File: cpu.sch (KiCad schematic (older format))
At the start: 26 parts, among them SW1 RESET, U1 74HC04, U2 Z80CPU, Y1 7.3728MHz

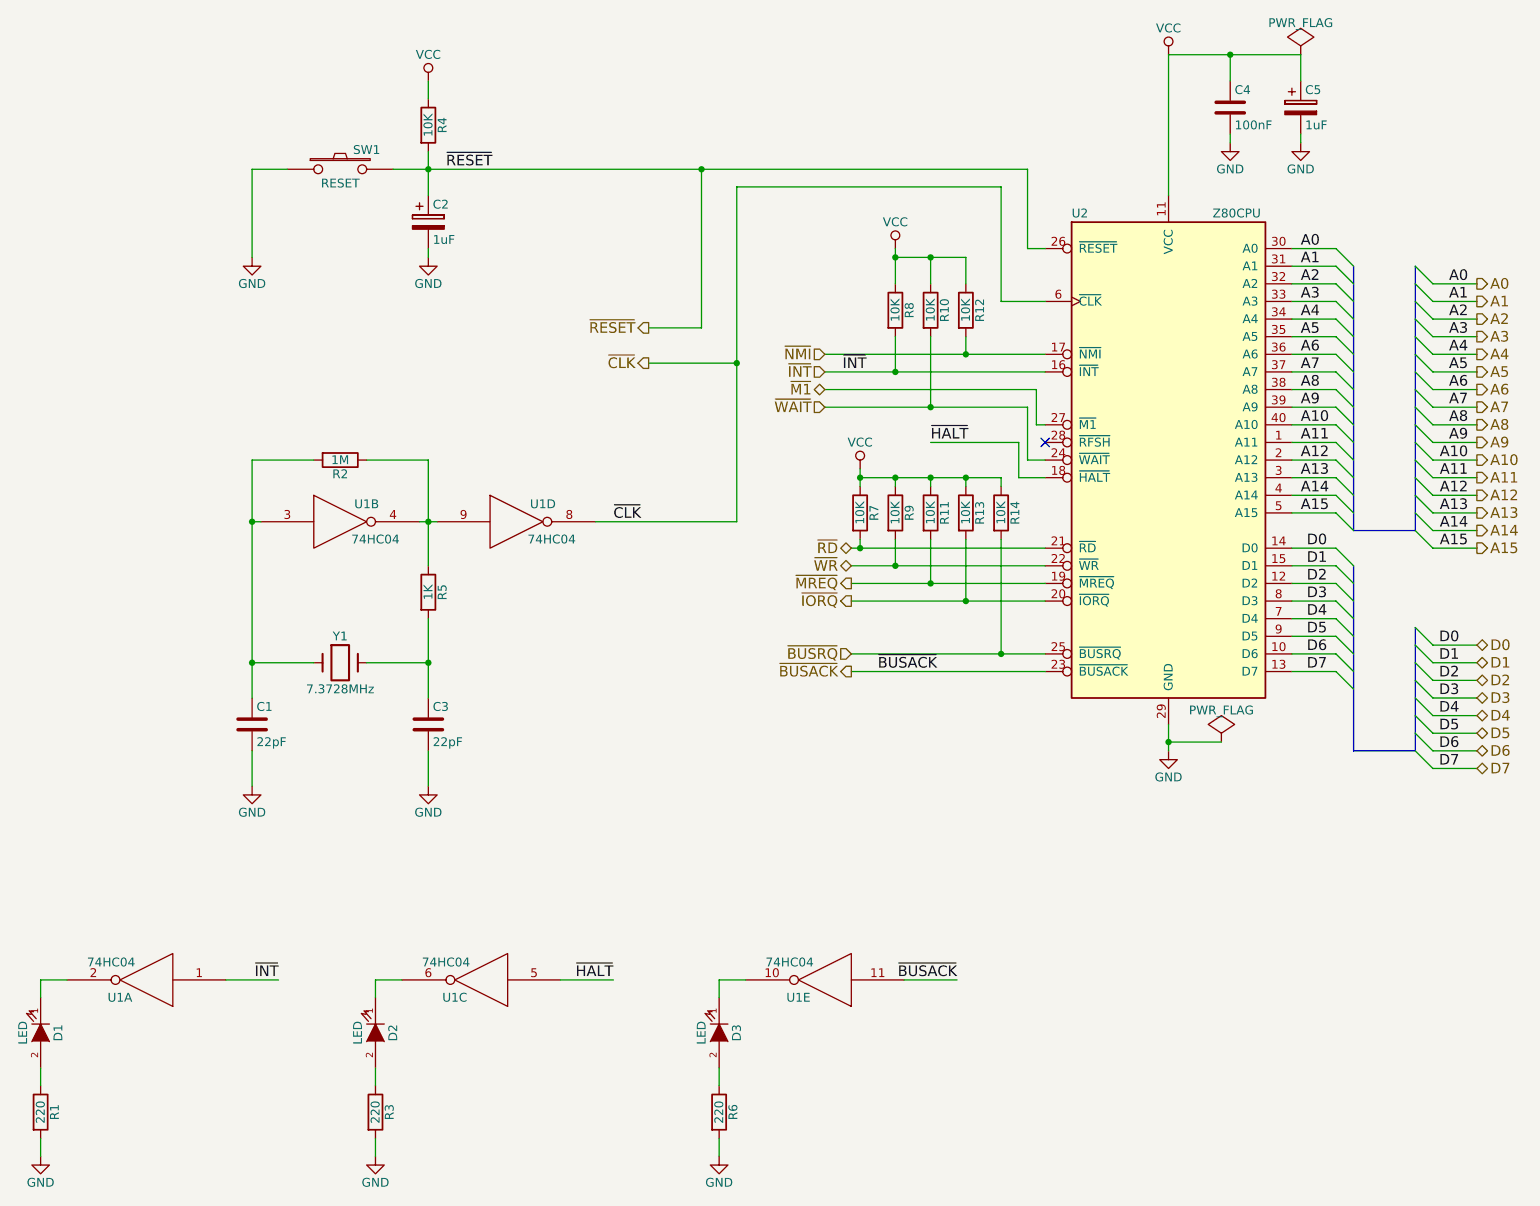
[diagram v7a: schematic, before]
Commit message: Added /intack signal and a pri-encoder for /iosel
Brain fart on the diode crap. Was tired. Added a priority encoder to
enable the Dx buffer so it properly tristates when no IObus ports are
selected.

Added a NOR gate to provide a /intack signal for any board to properly
detect their interupt has been accepted but the z80. Boards will need to
figure out who the interupt is for.

Will have to add interupt priority pins to the boards to allow the
boards to put jump vectors onto the data bus to service the interrupt
This should be fairly easy, just means the service pritority of the
slots will be A-H, with A being the highest priority and H being the
lowest.

Going to replace the hex inverters with the spare NOR gates too.
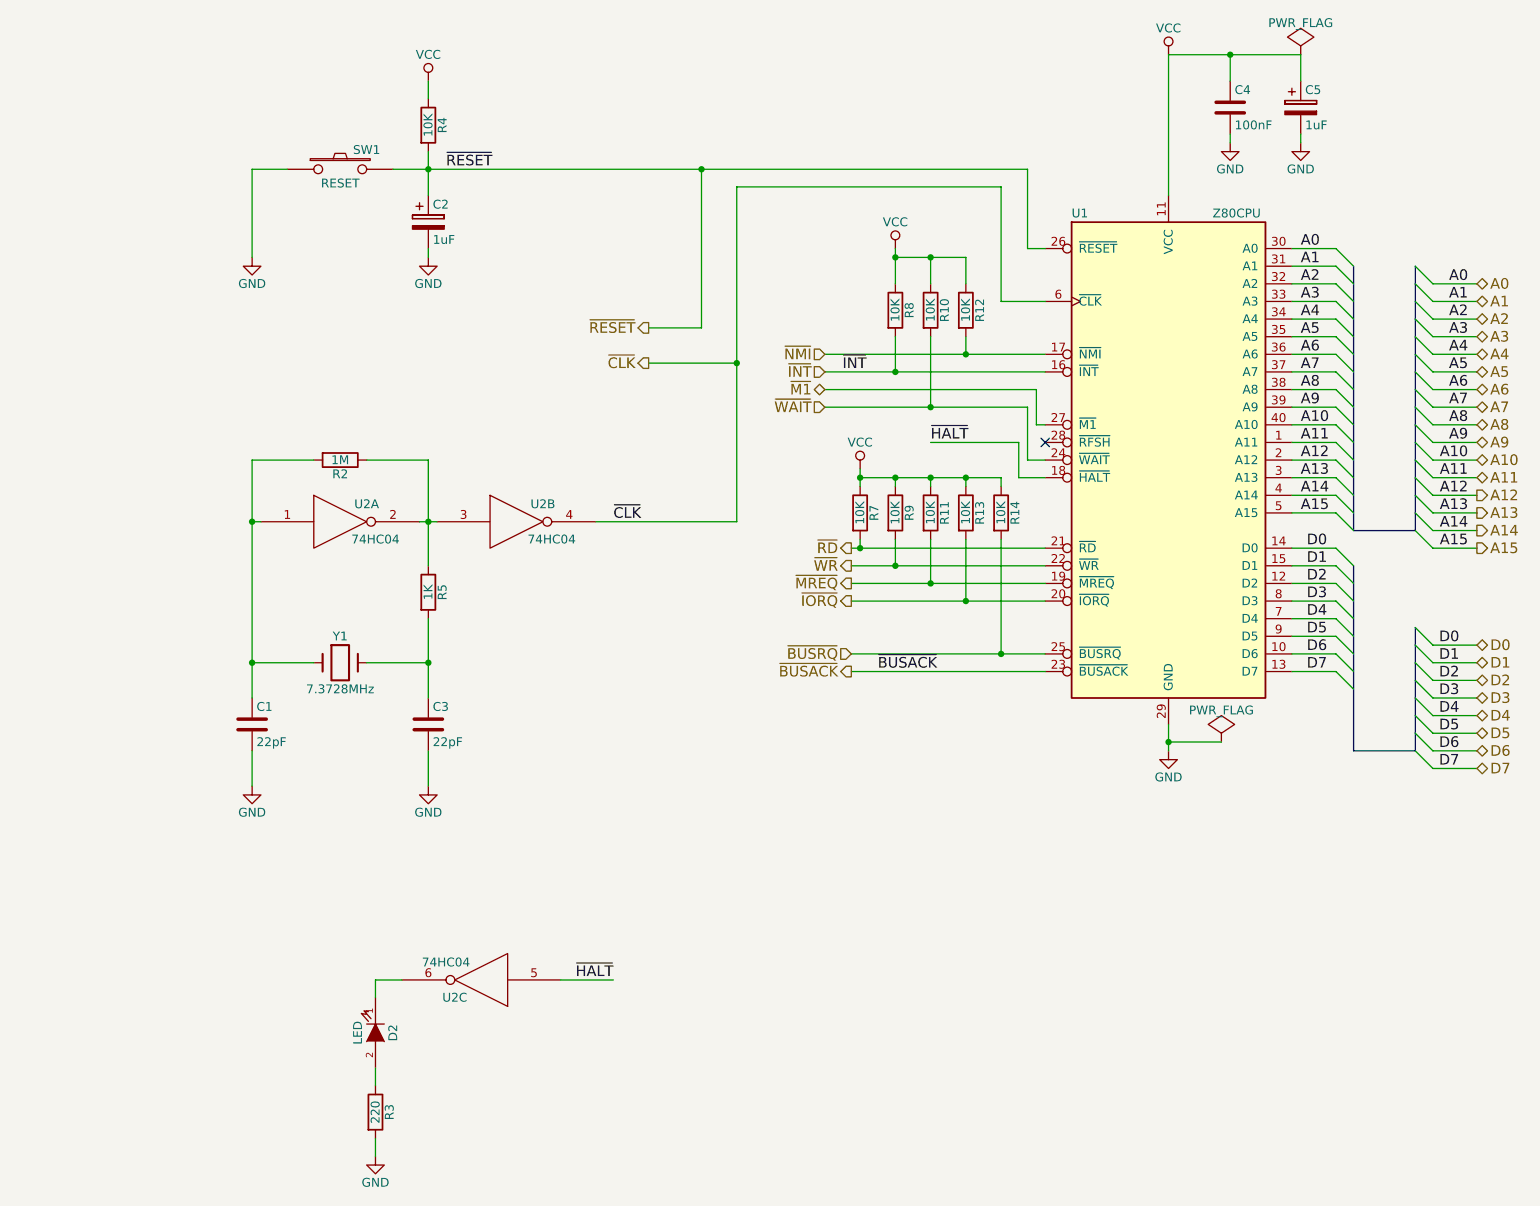
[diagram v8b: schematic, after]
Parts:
- removed D1, D3: LED, LEDs:LED-3MM, symbol LED
- removed R1, R6: 220, Resistors_SMD:R_0805_HandSoldering, symbol R
- removed unit 1 of U1
- removed unit 5 of U1
- renumbered U2 to U1, U1 to U2
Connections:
- net ~CLK: now also U2.4; no longer U2.8
- net at R2.1, R5.1: now also U2.2, U2.3; no longer U2.4, U2.9
- net at C1.1, R2.2, Y1.1: now also U2.1; no longer U2.3
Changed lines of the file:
@@
 $Descr A4 11693 8268
 encoding utf-8
-Sheet 2 16
+Sheet 2 14
 Title ""
 Date ""
@@
 $EndDescr
 $Comp
-L Z80CPU U2
+L Z80CPU U1
 U 1 1 577A4BA5
 P 8250 3050
-F 0 "U2" H 7700 4450 50  0000 L CNN
+F 0 "U1" H 7700 4450 50  0000 L CNN
 F 1 "Z80CPU" H 8500 4450 50  0000 L CNN
 F 2 "Housings_DIP:DIP-40_W25.4mm_LongPads" H 8250 3450 50  0001 C CNN
@@
 Wire Wire Line
 	9750 3550 10000 3550
-Text HLabel 10000 2050 2    60   Output ~ 0
+Text HLabel 10000 2050 2    60   3State ~ 0
 A0
-Text HLabel 10000 2150 2    60   Output ~ 0
+Text HLabel 10000 2150 2    60   3State ~ 0
 A1
-Text HLabel 10000 2250 2    60   Output ~ 0
+Text HLabel 10000 2250 2    60   3State ~ 0
 A2
-Text HLabel 10000 2350 2    60   Output ~ 0
+Text HLabel 10000 2350 2    60   3State ~ 0
 A3
-Text HLabel 10000 2450 2    60   Output ~ 0
+Text HLabel 10000 2450 2    60   3State ~ 0
 A4
-Text HLabel 10000 2550 2    60   Output ~ 0
+Text HLabel 10000 2550 2    60   3State ~ 0
 A5
-Text HLabel 10000 2650 2    60   Output ~ 0
+Text HLabel 10000 2650 2    60   3State ~ 0
 A6
-Text HLabel 10000 2750 2    60   Output ~ 0
+Text HLabel 10000 2750 2    60   3State ~ 0
 A7
-Text HLabel 10000 2850 2    60   Output ~ 0
+Text HLabel 10000 2850 2    60   3State ~ 0
 A8
-Text HLabel 10000 2950 2    60   Output ~ 0
+Text HLabel 10000 2950 2    60   3State ~ 0
 A9
-Text HLabel 10000 3050 2    60   Output ~ 0
+Text HLabel 10000 3050 2    60   3State ~ 0
 A10
-Text HLabel 10000 3150 2    60   Output ~ 0
+Text HLabel 10000 3150 2    60   3State ~ 0
 A11
 Text HLabel 10000 3250 2    60   Output ~ 0
@@
 	9650 4700 9300 4700
 $Comp
-L VCC #PWR9
+L VCC #PWR01
 U 1 1 577A5457
 P 6500 3100
-F 0 "#PWR9" H 6500 2950 50  0001 C CNN
+F 0 "#PWR01" H 6500 2950 50  0001 C CNN
 F 1 "VCC" H 6500 3250 50  0000 C CNN
 F 2 "" H 6500 3100 50  0000 C CNN
@@
 $EndComp
 $Comp
-L VCC #PWR10
+L VCC #PWR02
 U 1 1 577A54A8
 P 6700 1850
-F 0 "#PWR10" H 6700 1700 50  0001 C CNN
+F 0 "#PWR02" H 6700 1700 50  0001 C CNN
 F 1 "VCC" H 6700 2000 50  0000 C CNN
 F 2 "" H 6700 1850 50  0000 C CNN
@@
 	8250 1550 8250 750
 $Comp
-L VCC #PWR11
+L VCC #PWR03
 U 1 1 577A54FB
 P 8250 750
-F 0 "#PWR11" H 8250 600 50  0001 C CNN
+F 0 "#PWR03" H 8250 600 50  0001 C CNN
 F 1 "VCC" H 8250 900 50  0000 C CNN
 F 2 "" H 8250 750 50  0000 C CNN
@@
 	8250 4550 8250 4700
 $Comp
-L GND #PWR12
+L GND #PWR04
 U 1 1 577A554F
 P 8250 4700
-F 0 "#PWR12" H 8250 4450 50  0001 C CNN
+F 0 "#PWR04" H 8250 4450 50  0001 C CNN
 F 1 "GND" H 8250 4550 50  0000 C CNN
 F 2 "" H 8250 4700 50  0000 C CNN
@@
 	1    0    0    -1
 $EndComp
-Text HLabel 6450 3550 0    60   3State ~ 0
+Text HLabel 6450 3550 0    60   Output ~ 0
 ~RD
-Text HLabel 6450 3650 0    60   3State ~ 0
+Text HLabel 6450 3650 0    60   Output ~ 0
 ~WR
 Text HLabel 6300 2650 0    60   3State ~ 0
@@
 	7450 1400 3850 1400
 $Comp
-L 74HC04 U1
-U 4 1 577B1EB4
+L 74HC04 U2
+U 2 1 577B1EB4
 P 4550 3400
-F 0 "U1" H 4700 3500 50  0000 C CNN
+F 0 "U2" H 4700 3500 50  0000 C CNN
 F 1 "74HC04" H 4750 3300 50  0000 C CNN
 F 2 "Housings_DIP:DIP-14_W7.62mm_LongPads" H 4550 3400 50  0001 C CNN
 F 3 "" H 4550 3400 50  0000 C CNN
-	4    4550 3400
+	2    4550 3400
 	1    0    0    -1
 $EndComp
@@
 	5800 1500 5800 3400
 $Comp
-L 74HC04 U1
-U 2 1 577B20BC
+L 74HC04 U2
+U 1 1 577B20BC
 P 3550 3400
-F 0 "U1" H 3700 3500 50  0000 C CNN
+F 0 "U2" H 3700 3500 50  0000 C CNN
 F 1 "74HC04" H 3750 3300 50  0000 C CNN
 F 2 "Housings_DIP:DIP-14_W7.62mm_LongPads" H 3550 3400 50  0001 C CNN
 F 3 "" H 3550 3400 50  0000 C CNN
-	2    3550 3400
+	1    3550 3400
 	1    0    0    -1
 $EndComp
@@
 	4050 4700 4050 4900
 $Comp
-L GND #PWR3
+L GND #PWR05
 U 1 1 577B2CBE
 P 3050 4900
-F 0 "#PWR3" H 3050 4650 50  0001 C CNN
+F 0 "#PWR05" H 3050 4650 50  0001 C CNN
 F 1 "GND" H 3050 4750 50  0000 C CNN
 F 2 "" H 3050 4900 50  0000 C CNN
@@
 $EndComp
 $Comp
-L GND #PWR7
+L GND #PWR06
 U 1 1 577B2D0B
 P 4050 4900
-F 0 "#PWR7" H 4050 4650 50  0001 C CNN
+F 0 "#PWR06" H 4050 4650 50  0001 C CNN
 F 1 "GND" H 4050 4750 50  0000 C CNN
 F 2 "" H 4050 4900 50  0000 C CNN
@@
 $EndComp
 $Comp
-L 74HC04 U1
+L 74HC04 U2
 U 3 1 577B33CF
 P 4350 6000
-F 0 "U1" H 4500 6100 50  0000 C CNN
+F 0 "U2" H 4500 6100 50  0000 C CNN
 F 1 "74HC04" H 4550 5900 50  0000 C CNN
 F 2 "Housings_DIP:DIP-14_W7.62mm_LongPads" H 4350 6000 50  0001 C CNN
@@
 $EndComp
 $Comp
-L GND #PWR4
+L GND #PWR07
 U 1 1 577B377E
 P 3750 7000
-F 0 "#PWR4" H 3750 6750 50  0001 C CNN
+F 0 "#PWR07" H 3750 6750 50  0001 C CNN
 F 1 "GND" H 3750 6850 50  0000 C CNN
 F 2 "" H 3750 7000 50  0000 C CNN
@@
 	3050 1400 3050 1900
 $Comp
-L GND #PWR2
+L GND #PWR08
 U 1 1 577B455D
 P 3050 1900
-F 0 "#PWR2" H 3050 1650 50  0001 C CNN
+F 0 "#PWR08" H 3050 1650 50  0001 C CNN
 F 1 "GND" H 3050 1750 50  0000 C CNN
 F 2 "" H 3050 1900 50  0000 C CNN
@@
 	4050 1850 4050 1900
 $Comp
-L GND #PWR6
+L GND #PWR09
 U 1 1 577B48FE
 P 4050 1900
-F 0 "#PWR6" H 4050 1650 50  0001 C CNN
+F 0 "#PWR09" H 4050 1650 50  0001 C CNN
 F 1 "GND" H 4050 1750 50  0000 C CNN
 F 2 "" H 4050 1900 50  0000 C CNN
@@
 Text Label 6400 2550 0    60   ~ 0
 ~INT
-$Comp
-L 74HC04 U1
-U 1 1 577B4AF8
-P 2450 6000
-F 0 "U1" H 2600 6100 50  0000 C CNN
-F 1 "74HC04" H 2650 5900 50  0000 C CNN
-F 2 "Housings_DIP:DIP-14_W7.62mm_LongPads" H 2450 6000 50  0001 C CNN
-F 3 "" H 2450 6000 50  0000 C CNN
-	1    2450 6000
-	-1   0    0    1
-$EndComp
-Wire Wire Line
-	2900 6000 3200 6000
-Text Label 3200 6000 2    60   ~ 0
-~INT
-$Comp
-L LED D1
-U 1 1 577B4B00
-P 1850 6300
-F 0 "D1" H 1850 6400 50  0000 C CNN
-F 1 "LED" H 1850 6200 50  0000 C CNN
-F 2 "LEDs:LED-3MM" H 1850 6300 50  0001 C CNN
-F 3 "" H 1850 6300 50  0000 C CNN
-	1    1850 6300
-	0    1    1    0
-$EndComp
-$Comp
-L R R1
-U 1 1 577B4B06
-P 1850 6750
-F 0 "R1" V 1930 6750 50  0000 C CNN
-F 1 "220" V 1850 6750 50  0000 C CNN
-F 2 "Resistors_SMD:R_0805_HandSoldering" V 1780 6750 50  0001 C CNN
-F 3 "" H 1850 6750 50  0000 C CNN
-	1    1850 6750
-	1    0    0    -1
-$EndComp
-$Comp
-L GND #PWR1
-U 1 1 577B4B0C
-P 1850 7000
-F 0 "#PWR1" H 1850 6750 50  0001 C CNN
-F 1 "GND" H 1850 6850 50  0000 C CNN
-F 2 "" H 1850 7000 50  0000 C CNN
-F 3 "" H 1850 7000 50  0000 C CNN
-	1    1850 7000
-	1    0    0    -1
-$EndComp
-Wire Wire Line
-	1850 6500 1850 6600
-Wire Wire Line
-	1850 6900 1850 7000
-Wire Wire Line
-	1850 6100 1850 6000
-Wire Wire Line
-	1850 6000 2000 6000
 $Comp
 L R R4
@@
 $EndComp
 $Comp
-L VCC #PWR5
+L VCC #PWR010
 U 1 1 577B4D04
 P 4050 900
-F 0 "#PWR5" H 4050 750 50  0001 C CNN
+F 0 "#PWR010" H 4050 750 50  0001 C CNN
 F 1 "VCC" H 4050 1050 50  0000 C CNN
 F 2 "" H 4050 900 50  0000 C CNN
@@
 Text Label 6600 4250 0    60   ~ 0
 ~BUSACK
-$Comp
-L 74HC04 U1
-U 5 1 577B52AB
-P 6300 6000
-F 0 "U1" H 6450 6100 50  0000 C CNN
-F 1 "74HC04" H 6500 5900 50  0000 C CNN
-F 2 "Housings_DIP:DIP-14_W7.62mm_LongPads" H 6300 6000 50  0001 C CNN
-F 3 "" H 6300 6000 50  0000 C CNN
-	5    6300 6000
-	-1   0    0    1
-$EndComp
-Wire Wire Line
-	6750 6000 7050 6000
-Text Label 7050 6000 2    60   ~ 0
-~BUSACK
-$Comp
-L LED D3
-U 1 1 577B52B3
-P 5700 6300
-F 0 "D3" H 5700 6400 50  0000 C CNN
-F 1 "LED" H 5700 6200 50  0000 C CNN
-F 2 "LEDs:LED-3MM" H 5700 6300 50  0001 C CNN
-F 3 "" H 5700 6300 50  0000 C CNN
-	1    5700 6300
-	0    1    1    0
-$EndComp
-$Comp
-L R R6
-U 1 1 577B52B9
-P 5700 6750
-F 0 "R6" V 5780 6750 50  0000 C CNN
-F 1 "220" V 5700 6750 50  0000 C CNN
-F 2 "Resistors_SMD:R_0805_HandSoldering" V 5630 6750 50  0001 C CNN
-F 3 "" H 5700 6750 50  0000 C CNN
-	1    5700 6750
-	1    0    0    -1
-$EndComp
-$Comp
-L GND #PWR8
-U 1 1 577B52BF
-P 5700 7000
-F 0 "#PWR8" H 5700 6750 50  0001 C CNN
-F 1 "GND" H 5700 6850 50  0000 C CNN
-F 2 "" H 5700 7000 50  0000 C CNN
-F 3 "" H 5700 7000 50  0000 C CNN
-	1    5700 7000
-	1    0    0    -1
-$EndComp
-Wire Wire Line
-	5700 6500 5700 6600
-Wire Wire Line
-	5700 6900 5700 7000
-Wire Wire Line
-	5700 6100 5700 6000
-Wire Wire Line
-	5700 6000 5850 6000
 $Comp
 L CP C5
@@
 Connection ~ 8600 750
 $Comp
-L GND #PWR13
+L GND #PWR011
 U 1 1 577B59DE
 P 8600 1250
-F 0 "#PWR13" H 8600 1000 50  0001 C CNN
+F 0 "#PWR011" H 8600 1000 50  0001 C CNN
 F 1 "GND" H 8600 1100 50  0000 C CNN
 F 2 "" H 8600 1250 50  0000 C CNN
@@
 $EndComp
 $Comp
-L GND #PWR14
+L GND #PWR012
 U 1 1 577B5A43
 P 9000 1250
-F 0 "#PWR14" H 9000 1000 50  0001 C CNN
+F 0 "#PWR012" H 9000 1000 50  0001 C CNN
 F 1 "GND" H 9000 1100 50  0000 C CNN
 F 2 "" H 9000 1250 50  0000 C CNN
@@
 ~RESET
 $Comp
-L PWR_FLAG #FLG2
+L PWR_FLAG #FLG013
 U 1 1 5780650C
 P 9000 750
-F 0 "#FLG2" H 9000 845 50  0001 C CNN
+F 0 "#FLG013" H 9000 845 50  0001 C CNN
 F 1 "PWR_FLAG" H 9000 930 50  0000 C CNN
 F 2 "" H 9000 750 50  0000 C CNN
@@
 $EndComp
 $Comp
-L PWR_FLAG #FLG1
+L PWR_FLAG #FLG014
 U 1 1 57806779
 P 8550 4650
-F 0 "#FLG1" H 8550 4745 50  0001 C CNN
+F 0 "#FLG014" H 8550 4745 50  0001 C CNN
 F 1 "PWR_FLAG" H 8550 4830 50  0000 C CNN
 F 2 "" H 8550 4650 50  0000 C CNN
